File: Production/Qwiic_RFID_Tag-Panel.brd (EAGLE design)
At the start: 175 x 117.3 mm, 942 parts, among them J1 Qwiic, J10 Qwiic, J11 Qwiic, J13 Qwiic, J14 Qwiic, J16 Qwiic, J17 Qwiic, J19 Qwiic, J2 Qwiic, J20 Qwiic, J22 Qwiic, J23 Qwiic, J25 Qwiic, J26 Qwiic, J28 Qwiic, J29 Qwiic, J31 Qwiic, J32 Qwiic, J34 Qwiic, J35 Qwiic, J37 Qwiic, J38 Qwiic, J4 Qwiic, J40 Qwiic, J41 Qwiic, J43 Qwiic, J44 Qwiic, J46 Qwiic, J47 Qwiic, J49 Qwiic, J5 Qwiic, J50 Qwiic, J52 Qwiic, J53 Qwiic, J55 Qwiic, J56 Qwiic, J58 Qwiic, J59 Qwiic, J61 Qwiic, J62 Qwiic, J64 Qwiic, J65 Qwiic, J67 Qwiic, J68 Qwiic, J7 Qwiic, J70 Qwiic, J71 Qwiic, J8 Qwiic, U1 ST25DV64KC, U10 ST25DV64KC, U11 ST25DV64KC, U12 ST25DV64KC, U13 ST25DV64KC, U14 ST25DV64KC, U15 ST25DV64KC, U16 ST25DV64KC, U17 ST25DV64KC, U18 ST25DV64KC, U19 ST25DV64KC, U2 ST25DV64KC, U20 ST25DV64KC, U21 ST25DV64KC, U22 ST25DV64KC, U23 ST25DV64KC, U24 ST25DV64KC, U3 ST25DV64KC, U4 ST25DV64KC, U5 ST25DV64KC, U6 ST25DV64KC, U7 ST25DV64KC, U8 ST25DV64KC, U9 ST25DV64KC

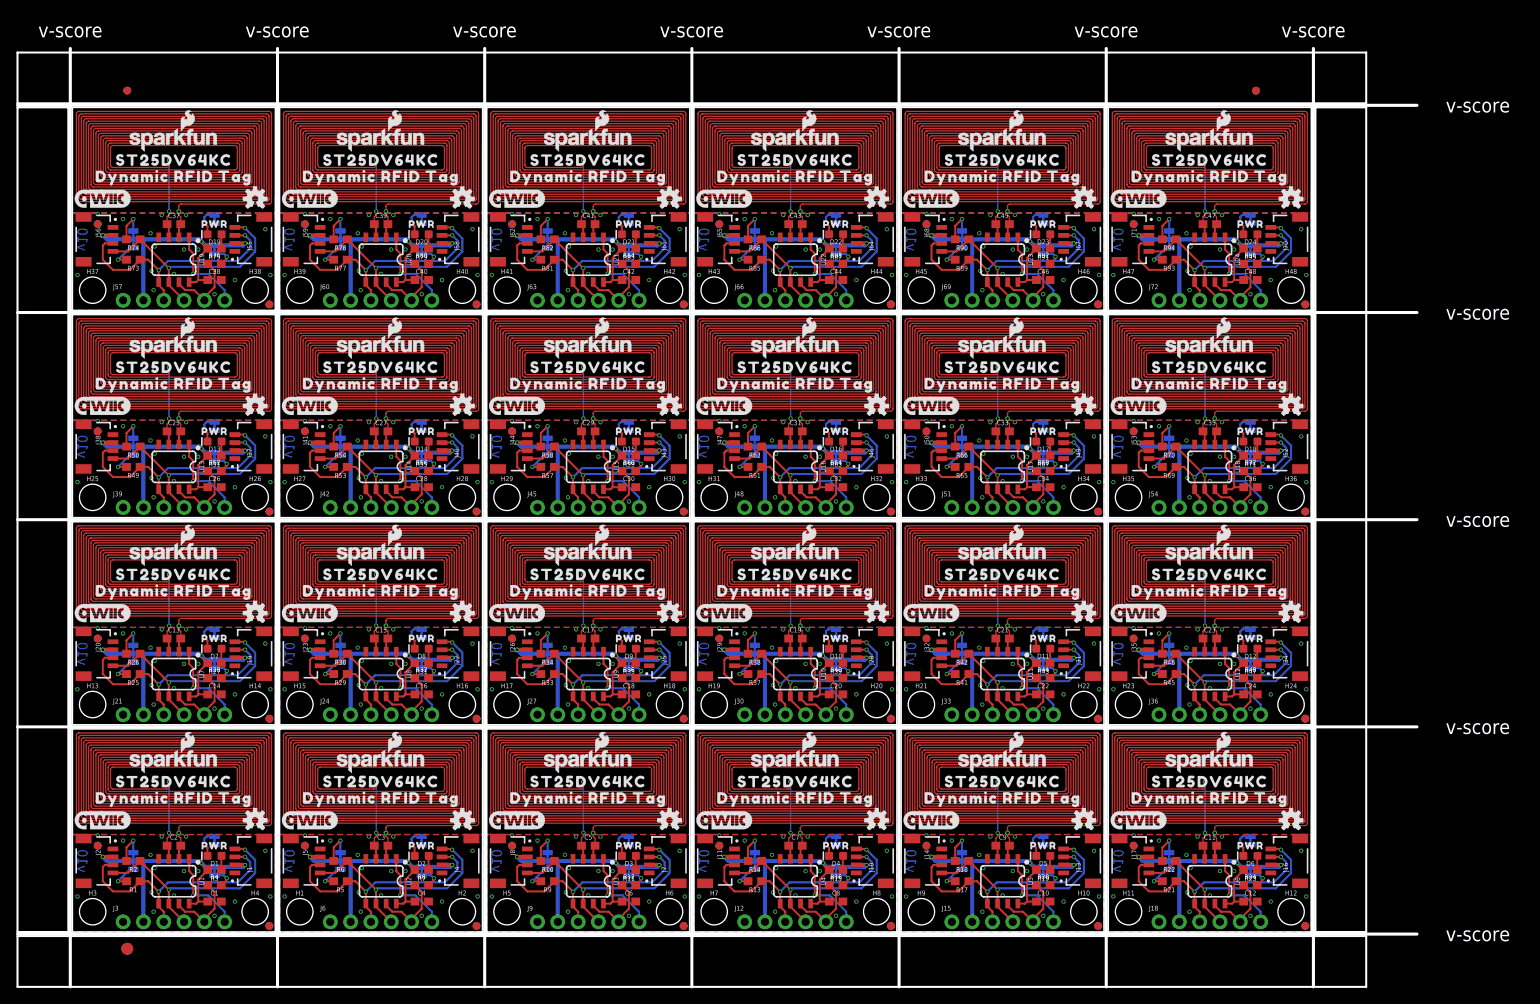
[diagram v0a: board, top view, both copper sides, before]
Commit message: Bump version number to v11 and repanelize
Panelizer didn't work correctly on v10, none of the pads had nets assigned to them, so the GND polygon didn't connect to any GND pads. Repanlizing seems to fix it? Idk, it's whacky.
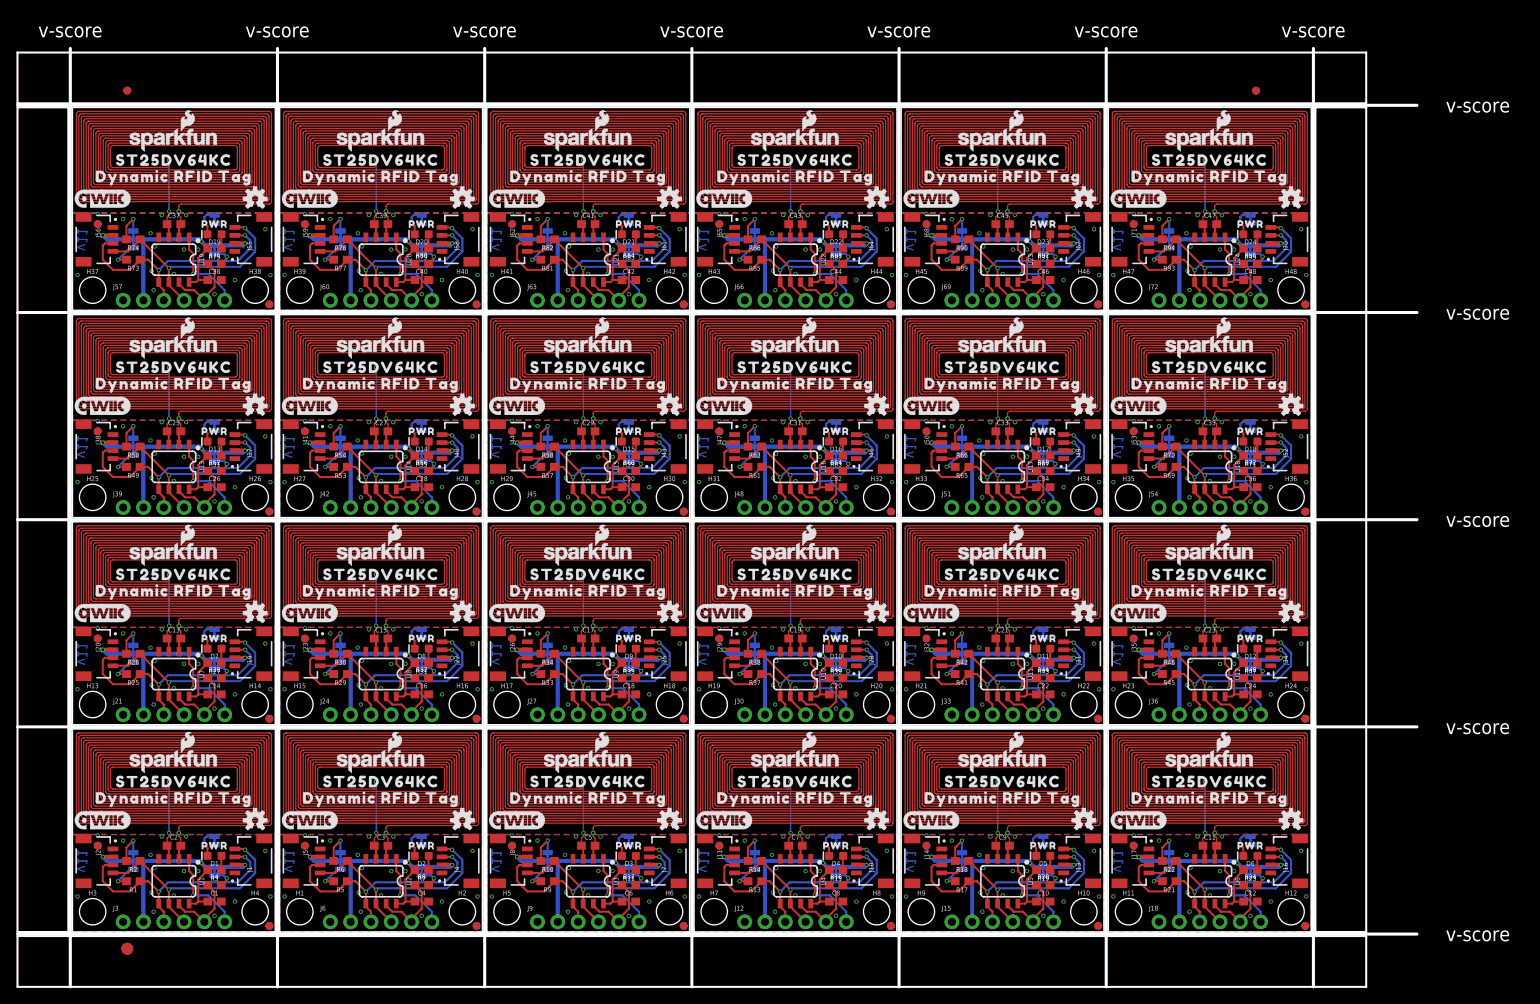
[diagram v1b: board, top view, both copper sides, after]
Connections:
- new net !GPO!: J3.5, R4.1, U1.7
- new net !GPO!1: J6.5, R8.1, U2.7
- new net !GPO!10: J33.5, R44.1, U11.7
- new net !GPO!11: J36.5, R48.1, U12.7
- new net !GPO!12: J39.5, R52.1, U13.7
- new net !GPO!13: J42.5, R56.1, U14.7
- new net !GPO!14: J45.5, R60.1, U15.7
- new net !GPO!15: J48.5, R64.1, U16.7
- new net !GPO!16: J51.5, R68.1, U17.7
- new net !GPO!17: J54.5, R72.1, U18.7
- new net !GPO!18: J57.5, R76.1, U19.7
- new net !GPO!19: J60.5, R80.1, U20.7
- new net !GPO!2: J9.5, R12.1, U3.7
- new net !GPO!20: J63.5, R84.1, U21.7
- new net !GPO!21: J66.5, R88.1, U22.7
- new net !GPO!22: J69.5, R92.1, U23.7
- new net !GPO!23: J72.5, R96.1, U24.7
- new net !GPO!3: J12.5, R16.1, U4.7
- new net !GPO!4: J15.5, R20.1, U5.7
- new net !GPO!5: J18.5, R24.1, U6.7
- new net !GPO!6: J21.5, R28.1, U7.7
- new net !GPO!7: J24.5, R32.1, U8.7
- new net !GPO!8: J27.5, R36.1, U9.7
- new net !GPO!9: J30.5, R40.1, U10.7
- new net 3.3V: C1.1, J1.2, J2.2, J3.2, JP1.2, JP2.2, R3.2, U1.8
- new net 3.3V1: C4.1, J4.2, J5.2, J6.2, JP4.2, JP6.2, R7.2, U2.8
- new net 3.3V10: C22.1, J31.2, J32.2, J33.2, JP31.2, JP33.2, R43.2, U11.8
- new net 3.3V11: C24.1, J34.2, J35.2, J36.2, JP34.2, JP36.2, R47.2, U12.8
- new net 3.3V12: C26.1, J37.2, J38.2, J39.2, JP37.2, JP39.2, R51.2, U13.8
- new net 3.3V13: C28.1, J40.2, J41.2, J42.2, JP40.2, JP42.2, R55.2, U14.8
- new net 3.3V14: C30.1, J43.2, J44.2, J45.2, JP43.2, JP45.2, R59.2, U15.8
- new net 3.3V15: C32.1, J46.2, J47.2, J48.2, JP46.2, JP48.2, R63.2, U16.8
- new net 3.3V16: C34.1, J49.2, J50.2, J51.2, JP49.2, JP51.2, R67.2, U17.8
- new net 3.3V17: C36.1, J52.2, J53.2, J54.2, JP52.2, JP54.2, R71.2, U18.8
- new net 3.3V18: C38.1, J55.2, J56.2, J57.2, JP55.2, JP57.2, R75.2, U19.8
- new net 3.3V19: C40.1, J58.2, J59.2, J60.2, JP58.2, JP60.2, R79.2, U20.8
- new net 3.3V2: C6.1, J7.2, J8.2, J9.2, JP7.2, JP9.2, R11.2, U3.8
- new net 3.3V20: C42.1, J61.2, J62.2, J63.2, JP61.2, JP63.2, R83.2, U21.8
- new net 3.3V21: C44.1, J64.2, J65.2, J66.2, JP64.2, JP66.2, R87.2, U22.8
- new net 3.3V22: C46.1, J67.2, J68.2, J69.2, JP67.2, JP69.2, R91.2, U23.8
- new net 3.3V23: C48.1, J70.2, J71.2, J72.2, JP70.2, JP72.2, R95.2, U24.8
- new net 3.3V3: C8.1, J10.2, J11.2, J12.2, JP10.2, JP12.2, R15.2, U4.8
- new net 3.3V4: C10.1, J13.2, J14.2, J15.2, JP13.2, JP15.2, R19.2, U5.8
- new net 3.3V5: C12.1, J16.2, J17.2, J18.2, JP16.2, JP18.2, R23.2, U6.8
- new net 3.3V6: C14.1, J19.2, J20.2, J21.2, JP19.2, JP21.2, R27.2, U7.8
- new net 3.3V7: C16.1, J22.2, J23.2, J24.2, JP22.2, JP24.2, R31.2, U8.8
- new net 3.3V8: C18.1, J25.2, J26.2, J27.2, JP25.2, JP27.2, R35.2, U9.8
- new net 3.3V9: C20.1, J28.2, J29.2, J30.2, JP28.2, JP30.2, R39.2, U10.8
- new net AC0: C2.2, L1.IN2, U1.2
- new net AC1: C2.1, L1.IN1, U1.3
- new net AC10: C11.2, L6.IN2, U6.2
- new net AC11: C11.1, L6.IN1, U6.3
- new net AC12: C13.2, L7.IN2, U7.2
- new net AC13: C13.1, L7.IN1, U7.3
- new net AC14: C15.2, L8.IN2, U8.2
- new net AC15: C15.1, L8.IN1, U8.3
- new net AC16: C17.2, L9.IN2, U9.2
- new net AC17: C17.1, L9.IN1, U9.3
- new net AC18: C19.2, L10.IN2, U10.2
- new net AC19: C19.1, L10.IN1, U10.3
- new net AC2: C3.2, L2.IN2, U2.2
- new net AC20: C21.2, L11.IN2, U11.2
- new net AC21: C21.1, L11.IN1, U11.3
- new net AC22: C23.2, L12.IN2, U12.2
- new net AC23: C23.1, L12.IN1, U12.3
- new net AC24: C25.2, L13.IN2, U13.2
- new net AC25: C25.1, L13.IN1, U13.3
- new net AC26: C27.2, L14.IN2, U14.2
- new net AC27: C27.1, L14.IN1, U14.3
- new net AC28: C29.2, L15.IN2, U15.2
- new net AC29: C29.1, L15.IN1, U15.3
- new net AC3: C3.1, L2.IN1, U2.3
- new net AC30: C31.2, L16.IN2, U16.2
- new net AC31: C31.1, L16.IN1, U16.3
- new net AC32: C33.2, L17.IN2, U17.2
- new net AC33: C33.1, L17.IN1, U17.3
- new net AC34: C35.2, L18.IN2, U18.2
- new net AC35: C35.1, L18.IN1, U18.3
- new net AC36: C37.2, L19.IN2, U19.2
- new net AC37: C37.1, L19.IN1, U19.3
- new net AC38: C39.2, L20.IN2, U20.2
- new net AC39: C39.1, L20.IN1, U20.3
- new net AC4: C5.2, L3.IN2, U3.2
- new net AC40: C41.2, L21.IN2, U21.2
- new net AC41: C41.1, L21.IN1, U21.3
- new net AC42: C43.2, L22.IN2, U22.2
- new net AC43: C43.1, L22.IN1, U22.3
- new net AC44: C45.2, L23.IN2, U23.2
- new net AC45: C45.1, L23.IN1, U23.3
- new net AC46: C47.2, L24.IN2, U24.2
- new net AC47: C47.1, L24.IN1, U24.3
- new net AC5: C5.1, L3.IN1, U3.3
- new net AC6: C7.2, L4.IN2, U4.2
- new net AC7: C7.1, L4.IN1, U4.3
- new net AC8: C9.2, L5.IN2, U5.2
- new net AC9: C9.1, L5.IN1, U5.3
- new net GND: C1.2, J1.1, J2.1, J3.1, JP3.1, U1.4
- new net GND1: C4.2, J4.1, J5.1, J6.1, JP5.1, U2.4
- new net GND10: C22.2, J31.1, J32.1, J33.1, JP32.1, U11.4
- new net GND11: C24.2, J34.1, J35.1, J36.1, JP35.1, U12.4
- new net GND12: C26.2, J37.1, J38.1, J39.1, JP38.1, U13.4
- new net GND13: C28.2, J40.1, J41.1, J42.1, JP41.1, U14.4
- new net GND14: C30.2, J43.1, J44.1, J45.1, JP44.1, U15.4
- new net GND15: C32.2, J46.1, J47.1, J48.1, JP47.1, U16.4
- new net GND16: C34.2, J49.1, J50.1, J51.1, JP50.1, U17.4
- new net GND17: C36.2, J52.1, J53.1, J54.1, JP53.1, U18.4
- new net GND18: C38.2, J55.1, J56.1, J57.1, JP56.1, U19.4
- new net GND19: C40.2, J58.1, J59.1, J60.1, JP59.1, U20.4
- new net GND2: C6.2, J7.1, J8.1, J9.1, JP8.1, U3.4
- new net GND20: C42.2, J61.1, J62.1, J63.1, JP62.1, U21.4
- new net GND21: C44.2, J64.1, J65.1, J66.1, JP65.1, U22.4
- new net GND22: C46.2, J67.1, J68.1, J69.1, JP68.1, U23.4
- new net GND23: C48.2, J70.1, J71.1, J72.1, JP71.1, U24.4
- new net GND3: C8.2, J10.1, J11.1, J12.1, JP11.1, U4.4
- new net GND4: C10.2, J13.1, J14.1, J15.1, JP14.1, U5.4
- new net GND5: C12.2, J16.1, J17.1, J18.1, JP17.1, U6.4
- new net GND6: C14.2, J19.1, J20.1, J21.1, JP20.1, U7.4
- new net GND7: C16.2, J22.1, J23.1, J24.1, JP23.1, U8.4
- new net GND8: C18.2, J25.1, J26.1, J27.1, JP26.1, U9.4
- new net GND9: C20.2, J28.1, J29.1, J30.1, JP29.1, U10.4
- new net N$1: D1.C, JP3.2
- new net N$10: D2.C, JP5.2
- new net N$100: D20.C, JP59.2
- new net N$101: JP61.3, R81.2
- new net N$102: JP61.1, R82.2
- new net N$103: D21.A, R83.1
- new net N$104: JP63.1, R84.2
- new net N$105: D21.C, JP62.2
- new net N$106: JP64.3, R85.2
- new net N$107: JP64.1, R86.2
- new net N$108: D22.A, R87.1
- new net N$109: JP66.1, R88.2
- new net N$11: JP7.3, R9.2
- new net N$110: D22.C, JP65.2
- new net N$111: JP67.3, R89.2
- new net N$112: JP67.1, R90.2
- new net N$113: D23.A, R91.1
- new net N$114: JP69.1, R92.2
- new net N$115: D23.C, JP68.2
- new net N$116: JP70.3, R93.2
- new net N$117: JP70.1, R94.2
- new net N$118: D24.A, R95.1
- new net N$119: JP72.1, R96.2
- new net N$12: JP7.1, R10.2
- new net N$120: D24.C, JP71.2
- new net N$13: D3.A, R11.1
- new net N$14: JP9.1, R12.2
- new net N$15: D3.C, JP8.2
- new net N$16: JP10.3, R13.2
- new net N$17: JP10.1, R14.2
- new net N$18: D4.A, R15.1
- new net N$19: JP12.1, R16.2
- new net N$2: JP1.3, R1.2
- new net N$20: D4.C, JP11.2
- new net N$21: JP13.3, R17.2
- new net N$22: JP13.1, R18.2
- new net N$23: D5.A, R19.1
- new net N$24: JP15.1, R20.2
- new net N$25: D5.C, JP14.2
- new net N$26: JP16.3, R21.2
- new net N$27: JP16.1, R22.2
- new net N$28: D6.A, R23.1
- new net N$29: JP18.1, R24.2
- new net N$3: JP1.1, R2.2
- new net N$30: D6.C, JP17.2
- new net N$31: JP19.3, R25.2
- new net N$32: JP19.1, R26.2
- new net N$33: D7.A, R27.1
- new net N$34: JP21.1, R28.2
- new net N$35: D7.C, JP20.2
- new net N$36: JP22.3, R29.2
- new net N$37: JP22.1, R30.2
- new net N$38: D8.A, R31.1
- new net N$39: JP24.1, R32.2
- new net N$4: D1.A, R3.1
- new net N$40: D8.C, JP23.2
- new net N$41: JP25.3, R33.2
- new net N$42: JP25.1, R34.2
- new net N$43: D9.A, R35.1
- new net N$44: JP27.1, R36.2
- new net N$45: D9.C, JP26.2
- new net N$46: JP28.3, R37.2
- new net N$47: JP28.1, R38.2
- new net N$48: D10.A, R39.1
- new net N$49: JP30.1, R40.2
- new net N$5: JP2.1, R4.2
- new net N$50: D10.C, JP29.2
- new net N$51: JP31.3, R41.2
- new net N$52: JP31.1, R42.2
- new net N$53: D11.A, R43.1
- new net N$54: JP33.1, R44.2
- new net N$55: D11.C, JP32.2
- new net N$56: JP34.3, R45.2
- new net N$57: JP34.1, R46.2
- new net N$58: D12.A, R47.1
- new net N$59: JP36.1, R48.2
- new net N$6: JP4.3, R5.2
- new net N$60: D12.C, JP35.2
- new net N$61: JP37.3, R49.2
- new net N$62: JP37.1, R50.2
- new net N$63: D13.A, R51.1
- new net N$64: JP39.1, R52.2
- new net N$65: D13.C, JP38.2
- new net N$66: JP40.3, R53.2
- new net N$67: JP40.1, R54.2
- new net N$68: D14.A, R55.1
- new net N$69: JP42.1, R56.2
- new net N$7: JP4.1, R6.2
- new net N$70: D14.C, JP41.2
- new net N$71: JP43.3, R57.2
- new net N$72: JP43.1, R58.2
- new net N$73: D15.A, R59.1
- new net N$74: JP45.1, R60.2
- new net N$75: D15.C, JP44.2
- new net N$76: JP46.3, R61.2
- new net N$77: JP46.1, R62.2
- new net N$78: D16.A, R63.1
- new net N$79: JP48.1, R64.2
- new net N$8: D2.A, R7.1
- new net N$80: D16.C, JP47.2
- new net N$81: JP49.3, R65.2
- new net N$82: JP49.1, R66.2
- new net N$83: D17.A, R67.1
- new net N$84: JP51.1, R68.2
- new net N$85: D17.C, JP50.2
- new net N$86: JP52.3, R69.2
- new net N$87: JP52.1, R70.2
- new net N$88: D18.A, R71.1
- new net N$89: JP54.1, R72.2
- new net N$9: JP6.1, R8.2
- new net N$90: D18.C, JP53.2
- new net N$91: JP55.3, R73.2
- new net N$92: JP55.1, R74.2
- new net N$93: D19.A, R75.1
- new net N$94: JP57.1, R76.2
- new net N$95: D19.C, JP56.2
- new net N$96: JP58.3, R77.2
- new net N$97: JP58.1, R78.2
- new net N$98: D20.A, R79.1
- new net N$99: JP60.1, R80.2
- new net SCL: J1.4, J2.4, J3.4, R2.1, U1.6
- new net SCL1: J4.4, J5.4, J6.4, R6.1, U2.6
- new net SCL10: J31.4, J32.4, J33.4, R42.1, U11.6
- new net SCL11: J34.4, J35.4, J36.4, R46.1, U12.6
- new net SCL12: J37.4, J38.4, J39.4, R50.1, U13.6
- new net SCL13: J40.4, J41.4, J42.4, R54.1, U14.6
- new net SCL14: J43.4, J44.4, J45.4, R58.1, U15.6
- new net SCL15: J46.4, J47.4, J48.4, R62.1, U16.6
- new net SCL16: J49.4, J50.4, J51.4, R66.1, U17.6
- new net SCL17: J52.4, J53.4, J54.4, R70.1, U18.6
- new net SCL18: J55.4, J56.4, J57.4, R74.1, U19.6
- new net SCL19: J58.4, J59.4, J60.4, R78.1, U20.6
- new net SCL2: J7.4, J8.4, J9.4, R10.1, U3.6
- new net SCL20: J61.4, J62.4, J63.4, R82.1, U21.6
- new net SCL21: J64.4, J65.4, J66.4, R86.1, U22.6
- new net SCL22: J67.4, J68.4, J69.4, R90.1, U23.6
- new net SCL23: J70.4, J71.4, J72.4, R94.1, U24.6
- new net SCL3: J10.4, J11.4, J12.4, R14.1, U4.6
- new net SCL4: J13.4, J14.4, J15.4, R18.1, U5.6
- new net SCL5: J16.4, J17.4, J18.4, R22.1, U6.6
- new net SCL6: J19.4, J20.4, J21.4, R26.1, U7.6
- new net SCL7: J22.4, J23.4, J24.4, R30.1, U8.6
- new net SCL8: J25.4, J26.4, J27.4, R34.1, U9.6
- new net SCL9: J28.4, J29.4, J30.4, R38.1, U10.6
- new net SDA: J1.3, J2.3, J3.3, R1.1, U1.5
- new net SDA1: J4.3, J5.3, J6.3, R5.1, U2.5
- new net SDA10: J31.3, J32.3, J33.3, R41.1, U11.5
- new net SDA11: J34.3, J35.3, J36.3, R45.1, U12.5
- new net SDA12: J37.3, J38.3, J39.3, R49.1, U13.5
- new net SDA13: J40.3, J41.3, J42.3, R53.1, U14.5
- new net SDA14: J43.3, J44.3, J45.3, R57.1, U15.5
- new net SDA15: J46.3, J47.3, J48.3, R61.1, U16.5
- new net SDA16: J49.3, J50.3, J51.3, R65.1, U17.5
- new net SDA17: J52.3, J53.3, J54.3, R69.1, U18.5
- new net SDA18: J55.3, J56.3, J57.3, R73.1, U19.5
- new net SDA19: J58.3, J59.3, J60.3, R77.1, U20.5
- new net SDA2: J7.3, J8.3, J9.3, R9.1, U3.5
- new net SDA20: J61.3, J62.3, J63.3, R81.1, U21.5
- new net SDA21: J64.3, J65.3, J66.3, R85.1, U22.5
- new net SDA22: J67.3, J68.3, J69.3, R89.1, U23.5
- new net SDA23: J70.3, J71.3, J72.3, R93.1, U24.5
- new net SDA3: J10.3, J11.3, J12.3, R13.1, U4.5
- new net SDA4: J13.3, J14.3, J15.3, R17.1, U5.5
- new net SDA5: J16.3, J17.3, J18.3, R21.1, U6.5
- new net SDA6: J19.3, J20.3, J21.3, R25.1, U7.5
- new net SDA7: J22.3, J23.3, J24.3, R29.1, U8.5
- new net SDA8: J25.3, J26.3, J27.3, R33.1, U9.5
- new net SDA9: J28.3, J29.3, J30.3, R37.1, U10.5
- new net VEH: J3.6, U1.1
- new net VEH1: J6.6, U2.1
- new net VEH10: J33.6, U11.1
- new net VEH11: J36.6, U12.1
- new net VEH12: J39.6, U13.1
- new net VEH13: J42.6, U14.1
- new net VEH14: J45.6, U15.1
- new net VEH15: J48.6, U16.1
- new net VEH16: J51.6, U17.1
- new net VEH17: J54.6, U18.1
- new net VEH18: J57.6, U19.1
- new net VEH19: J60.6, U20.1
- new net VEH2: J9.6, U3.1
- new net VEH20: J63.6, U21.1
- new net VEH21: J66.6, U22.1
- new net VEH22: J69.6, U23.1
- new net VEH23: J72.6, U24.1
- new net VEH3: J12.6, U4.1
- new net VEH4: J15.6, U5.1
- new net VEH5: J18.6, U6.1
- new net VEH6: J21.6, U7.1
- new net VEH7: J24.6, U8.1
- new net VEH8: J27.6, U9.1
- new net VEH9: J30.6, U10.1
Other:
- board text added: "v11"
- board text removed: "v10"
